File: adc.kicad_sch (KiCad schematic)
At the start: 43 parts, among them J7 Conn_01x06_Female, U10 ADS7924, U11 PCT2075D, U5 LM4040DBZ-3, U6 ISO1540, U7 ADS7924, U8 LM3480-3.3, U9 LM4040DBZ-3

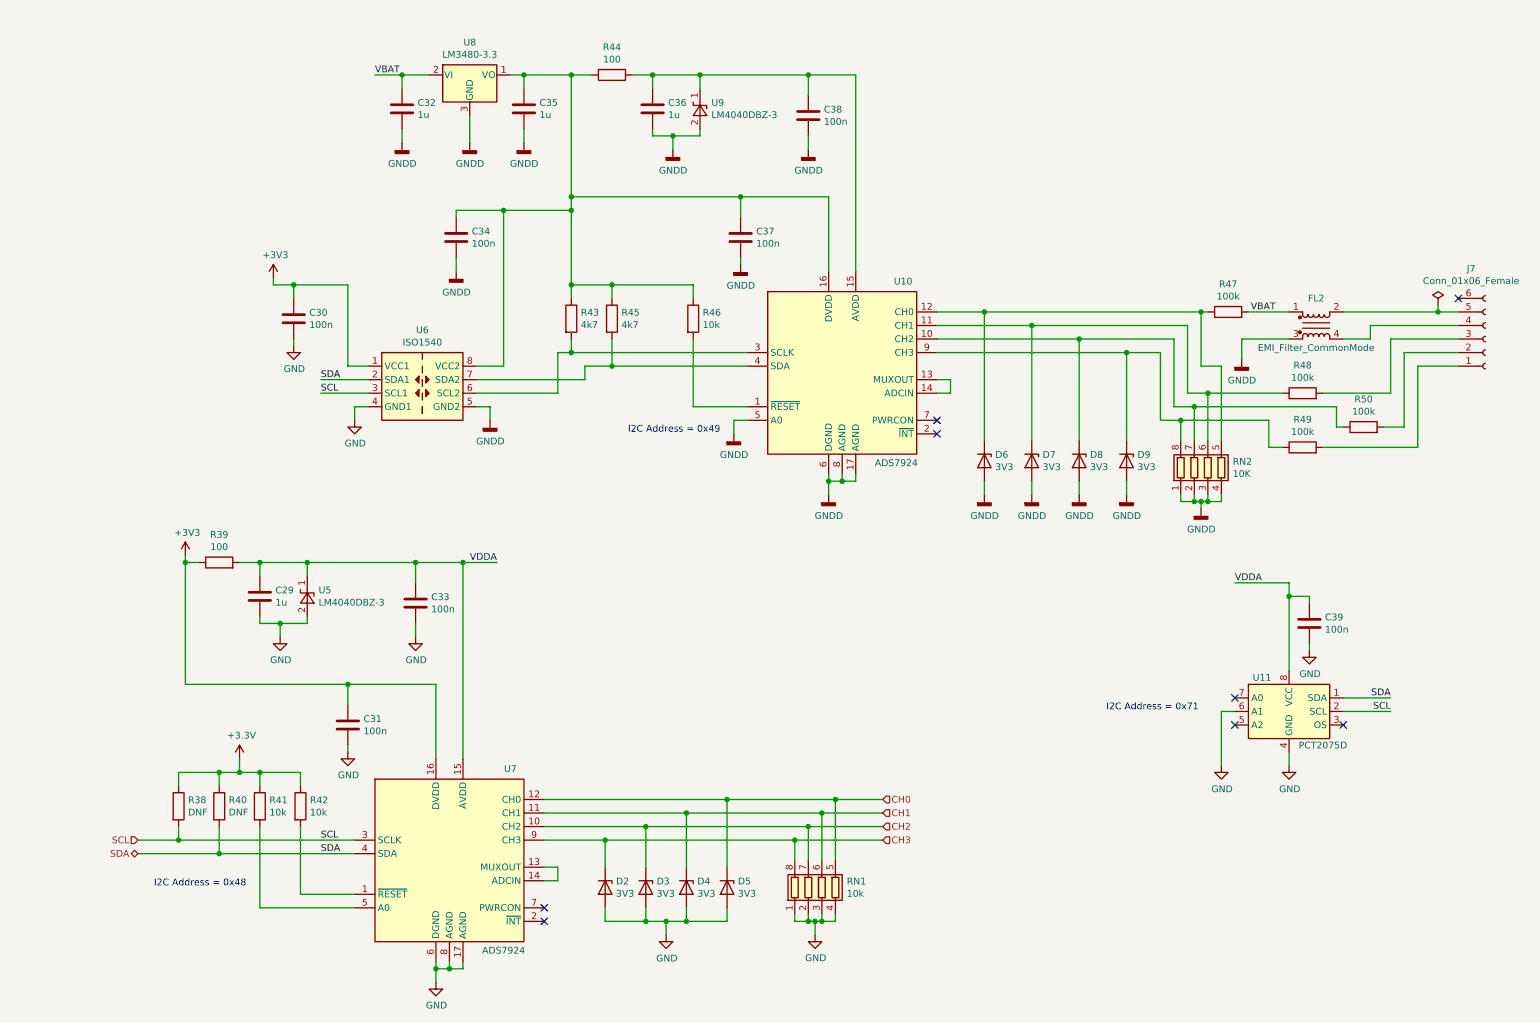
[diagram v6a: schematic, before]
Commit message: Tweaked component values to working. Added rear panel PCB
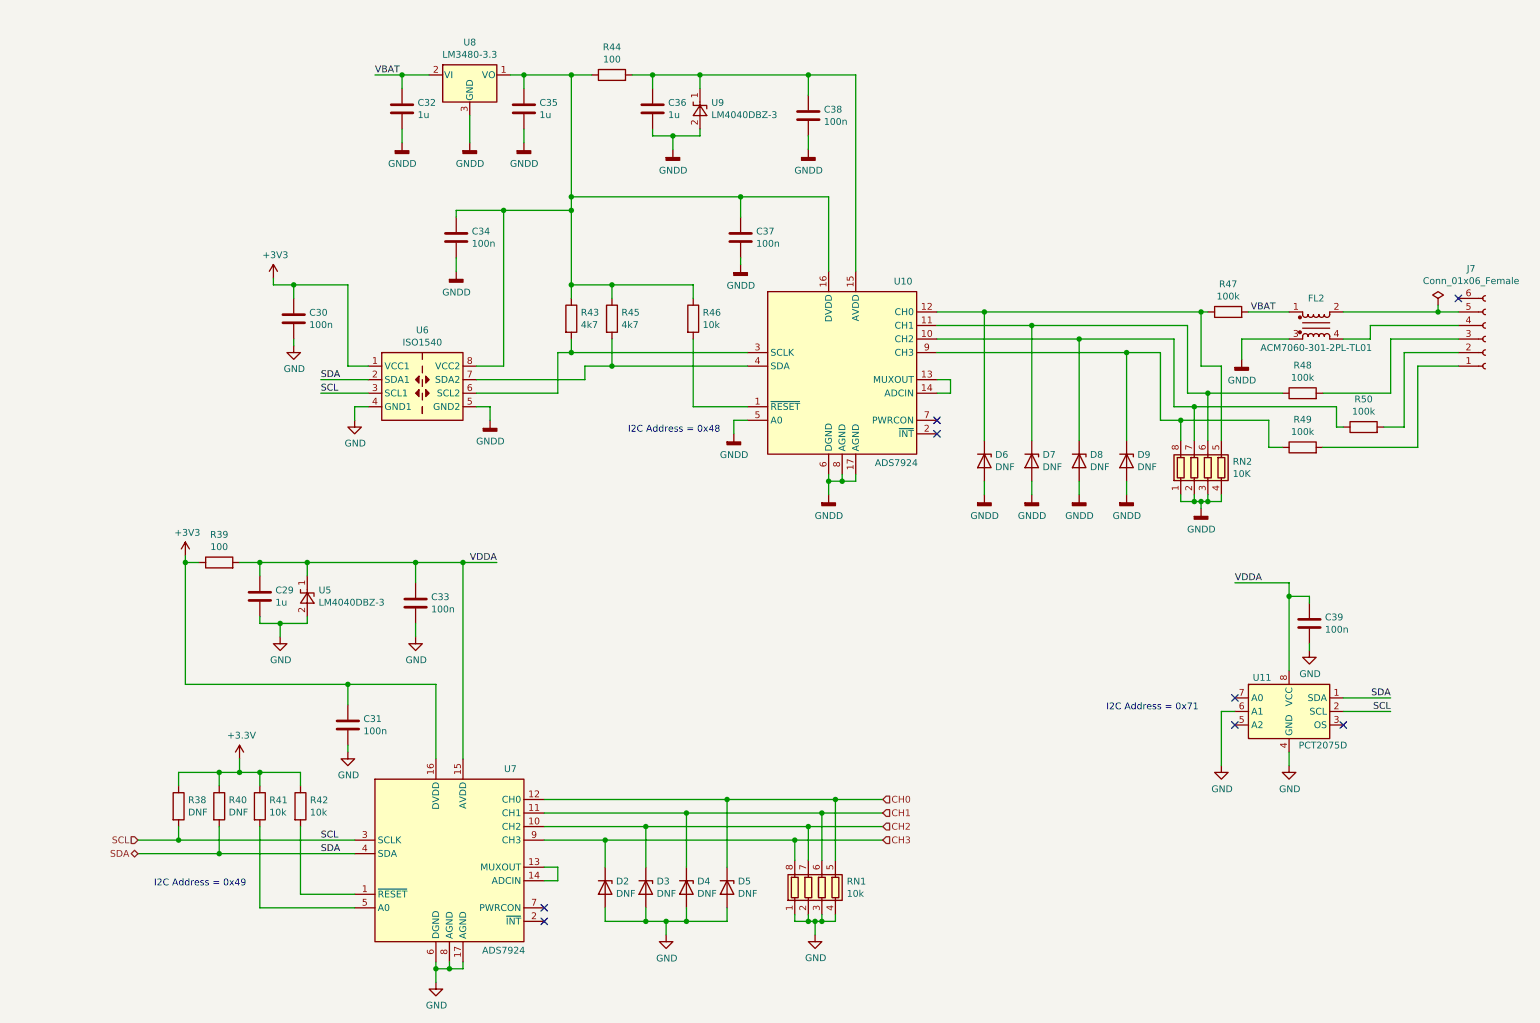
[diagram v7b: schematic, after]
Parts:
- D2, D3, D4, D5, D6, D7, D8, D9: value 3V3 -> DNF
- FL2: value EMI_Filter_CommonMode -> ACM7060-301-2PL-TL01
